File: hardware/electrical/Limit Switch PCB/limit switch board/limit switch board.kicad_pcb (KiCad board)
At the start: 2 copper layers, 29.2 x 15.6 mm, 2 parts, among them J1 Conn_01x02, J2 Conn_01x03

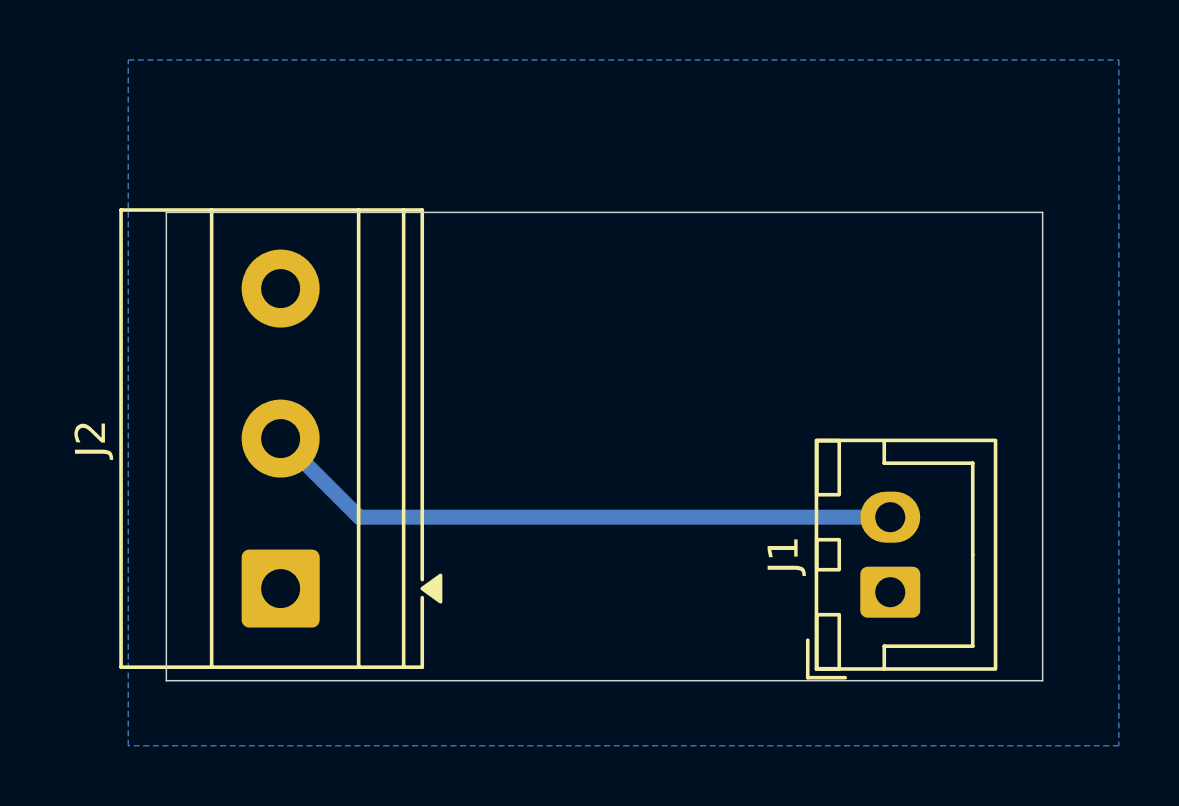
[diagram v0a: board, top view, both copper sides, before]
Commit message: backup sensor and limit switch PCBs
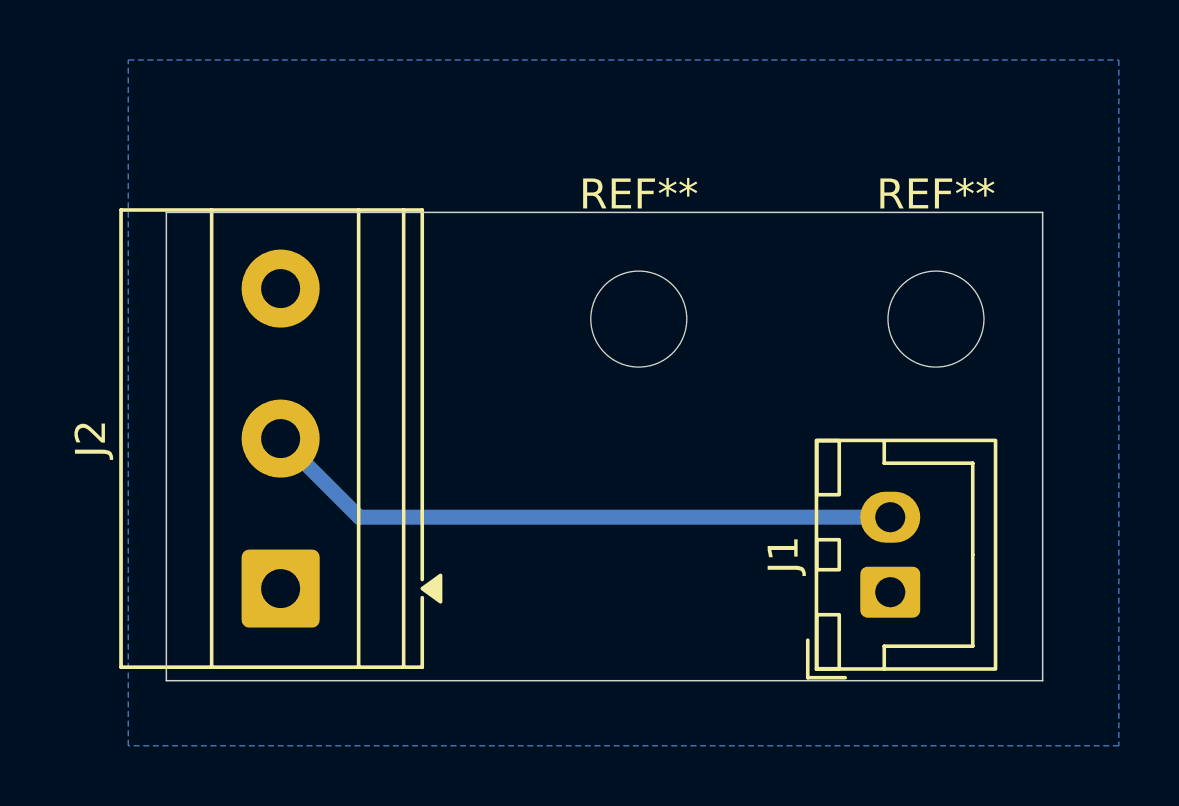
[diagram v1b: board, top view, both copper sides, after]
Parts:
- added REF**: MountingHole_3.2mm_M3, MountingHole:MountingHole_3.2mm_M3, F.Cu at (138.9, 87.4)
- added REF**: MountingHole_3.2mm_M3, MountingHole:MountingHole_3.2mm_M3, F.Cu at (148.8, 87.4)
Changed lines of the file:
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@@
 		(filling no)
 		(pcbplotparams
-			(layerselection 0x00000000_00000000_55555555_5755f5ff)
+			(layerselection 0x00000000_00000000_55555555_5755555e)
 			(plot_on_all_layers_selection 0x00000000_00000000_00000000_00000000)
 			(disableapertmacros no)
 			(usegerberextensions no)
-			(usegerberattributes yes)
-			(usegerberadvancedattributes yes)
+			(usegerberattributes no)
+			(usegerberadvancedattributes no)
 			(creategerberjobfile yes)
 			(dashed_line_dash_ratio 12)
@@
 			(outputformat 1)
 			(mirror no)
-			(drillshape 1)
+			(drillshape 0)
 			(scaleselection 1)
-			(outputdirectory "")
-		)
+			(outputdirectory "limit switch gerber/")
+		)
+	)
+	(footprint "MountingHole:MountingHole_3.2mm_M3"
+		(layer "F.Cu")
+		(at 138.938 87.376)
+		(descr "Mounting Hole 3.2mm, M3, no annular, generated by kicad-footprint-generator mountinghole.py")
+		(tags "mountinghole M3")
+		(property "Reference" "REF**"
+			(at 0 -4.15 0)
+			(layer "F.SilkS")
+			(effects
+				(font
+					(size 1 1)
+					(thickness 0.15)
+				)
+			)
+		)
+		(property "Value" "MountingHole_3.2mm_M3"
+			(at 0 4.15 0)
+			(layer "F.Fab")
+			(effects
+				(font
+					(size 1 1)
+					(thickness 0.15)
+				)
+			)
+		)
+		(property "Datasheet" ""
+			(at 0 0 0)
+			(layer "F.Fab")
+			(hide yes)
+			(effects
+				(font
+					(size 1.27 1.27)
+				)
+			)
+		)
+		(property "Description" ""
+			(at 0 0 0)
+			(layer "F.Fab")
+			(hide yes)
+			(effects
+				(font
+					(size 1.27 1.27)
+				)
+			)
+		)
+		(property "KiLib_Generator" "mounting_hardware/mounting_hole"
+			(at 0 0 0)
+			(layer "F.SilkS")
+			(hide yes)
+			(effects
+				(font
+					(size 1 1)
+					(thickness 0.15)
+				)
+			)
+		)
+		(attr exclude_from_pos_files exclude_from_bom)
+		(duplicate_pad_numbers_are_jumpers no)
+		(fp_circle
+			(center 0 0)
+			(end 3.2 0)
+			(stroke
+				(width 0.15)
+				(type solid)
+			)
+			(fill no)
+			(layer "Cmts.User")
+		)
+		(fp_circle
+			(center 0 0)
+			(end 3.45 0)
+			(stroke
+				(width 0.05)
+				(type solid)
+			)
+			(fill no)
+			(layer "F.CrtYd")
+		)
+		(fp_text user "${REFERENCE}"
+			(at 0 0 0)
+			(layer "F.Fab")
+			(effects
+				(font
+					(size 1 1)
+					(thickness 0.15)
+				)
+			)
+		)
+		(pad "" np_thru_hole circle
+			(at 0 0)
+			(size 3.2 3.2)
+			(drill 3.2)
+			(layers "*.Cu" "*.Mask")
+		)
+		(embedded_fonts no)
 	)
 	(footprint "TerminalBlock_Phoenix:TerminalBlock_Phoenix_MKDS-1,5-3_1x03_P5.00mm_Horizontal"
@@
 		)
 	)
+	(footprint "MountingHole:MountingHole_3.2mm_M3"
+		(layer "F.Cu")
+		(at 148.844 87.376)
+		(descr "Mounting Hole 3.2mm, M3, no annular, generated by kicad-footprint-generator mountinghole.py")
+		(tags "mountinghole M3")
+		(property "Reference" "REF**"
+			(at 0 -4.15 0)
+			(layer "F.SilkS")
+			(effects
+				(font
+					(size 1 1)
+					(thickness 0.15)
+				)
+			)
+		)
+		(property "Value" "MountingHole_3.2mm_M3"
+			(at 0 4.15 0)
+			(layer "F.Fab")
+			(effects
+				(font
+					(size 1 1)
+					(thickness 0.15)
+				)
+			)
+		)
+		(property "Datasheet" ""
+			(at 0 0 0)
+			(layer "F.Fab")
+			(hide yes)
+			(effects
+				(font
+					(size 1.27 1.27)
+				)
+			)
+		)
+		(property "Description" ""
+			(at 0 0 0)
+			(layer "F.Fab")
+			(hide yes)
+			(effects
+				(font
+					(size 1.27 1.27)
+				)
+			)
+		)
+		(property "KiLib_Generator" "mounting_hardware/mounting_hole"
+			(at 0 0 0)
+			(layer "F.SilkS")
+			(hide yes)
+			(effects
+				(font
+					(size 1 1)
+					(thickness 0.15)
+				)
+			)
+		)
+		(attr exclude_from_pos_files exclude_from_bom)
+		(duplicate_pad_numbers_are_jumpers no)
+		(fp_circle
+			(center 0 0)
+			(end 3.2 0)
+			(stroke
+				(width 0.15)
+				(type solid)
+			)
+			(fill no)
+			(layer "Cmts.User")
+		)
+		(fp_circle
+			(center 0 0)
+			(end 3.45 0)
+			(stroke
+				(width 0.05)
+				(type solid)
+			)
+			(fill no)
+			(layer "F.CrtYd")
+		)
+		(fp_text user "${REFERENCE}"
+			(at 0 0 0)
+			(layer "F.Fab")
+			(effects
+				(font
+					(size 1 1)
+					(thickness 0.15)
+				)
+			)
+		)
+		(pad "" np_thru_hole circle
+			(at 0 0)
+			(size 3.2 3.2)
+			(drill 3.2)
+			(layers "*.Cu" "*.Mask")
+		)
+		(embedded_fonts no)
+	)
 	(gr_rect
